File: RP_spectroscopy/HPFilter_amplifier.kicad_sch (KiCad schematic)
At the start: 0 parts

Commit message: Added components to the power supply branch. Implemented the Sallen-Key filter + amplification branch.
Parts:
- added C14, C15: 10n, symbol Device:C
- added R20, R21: 5K36, symbol Device:R
- added R22, R24: 1k, symbol Device:R
- added R23, R25: 7K32, symbol Device:R
- added R26: 49R9, symbol Device:R
- added U6: OPA1644, Package_SO:SOIC-14_3.9x8.7mm_P1.27mm, symbol Device:Opamp_Quad
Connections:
- new net: C14.2, C15.1, R20.1
- new net: C15.2, R21.1, U6.3 (+)
- new net: R22.1, R23.1, U6.6 (-)
- new net: R20.2, U6.1, U6.2 (-), U6.5 (+)
- new net: R23.2, U6.10 (+), U6.7
- new net: R25.2, R26.1, U6.8
- new net: R24.1, R25.1, U6.9 (-)
- new net +15V: U6.4 (V+)
- new net -15V: U6.11 (V-)
- new net GND: R21.2, R22.2, R24.2
- new net HPF + amplif: R26.2
- new net PD: C14.1
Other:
- note added: "Cascade amplification"
- note added: "Sallen-Key filter in HP configuration"

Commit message: Commit before deleting the VCO schematic from the main project. I have a separate project for that.
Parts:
- C14, C15: footprint (none) -> Capacitor_SMD:C_0805_2012Metric_Pad1.18x1.45mm_HandSolder
- R20, R21, R22, R23, R24, R25, R26: footprint (none) -> Resistor_SMD:R_0805_2012Metric_Pad1.20x1.40mm_HandSolder
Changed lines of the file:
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@@
 			)
 		)
-		(property "Footprint" ""
+		(property "Footprint" "Capacitor_SMD:C_0805_2012Metric_Pad1.18x1.45mm_HandSolder"
 			(at 101.6 79.0448 0)
 			(effects
@@
 			)
 		)
-		(property "Description" "Unpolarized capacitor"
+		(property "Description" "Unpolarized capacitor, 10n C0G 50V"
 			(at 97.79 80.01 0)
 			(effects
@@
 			)
 		)
-		(property "Footprint" ""
+		(property "Footprint" "Resistor_SMD:R_0805_2012Metric_Pad1.20x1.40mm_HandSolder"
 			(at 103.632 87.63 90)
 			(effects
@@
 			)
 		)
-		(property "Description" "Resistor"
+		(property "Description" "Resistor, 5k36 1%"
 			(at 105.41 87.63 0)
 			(effects
@@
 			)
 		)
-		(property "Footprint" ""
+		(property "Footprint" "Resistor_SMD:R_0805_2012Metric_Pad1.20x1.40mm_HandSolder"
 			(at 151.892 104.14 90)
 			(effects
@@
 			)
 		)
-		(property "Description" "Resistor"
+		(property "Description" "Resistor, 1k 1%"
 			(at 153.67 104.14 0)
 			(effects
@@
 			)
 		)
-		(property "Footprint" ""
+		(property "Footprint" "Resistor_SMD:R_0805_2012Metric_Pad1.20x1.40mm_HandSolder"
 			(at 217.17 89.408 90)
 			(effects
@@
 			)
 		)
-		(property "Description" "Resistor"
+		(property "Description" "Resistor, 49R9 1%"
 			(at 217.17 87.63 0)
 			(effects
@@
 			)
 		)
-		(property "Footprint" ""
+		(property "Footprint" "Resistor_SMD:R_0805_2012Metric_Pad1.20x1.40mm_HandSolder"
 			(at 200.66 100.838 90)
 			(effects
@@
 			)
 		)
-		(property "Description" "Resistor"
+		(property "Description" "Resistor, 7k32 1%"
 			(at 200.66 99.06 0)
 			(effects
@@
 			)
 		)
-		(property "Footprint" ""
+		(property "Footprint" "Resistor_SMD:R_0805_2012Metric_Pad1.20x1.40mm_HandSolder"
 			(at 113.03 71.628 90)
 			(effects
@@
 			)
 		)
-		(property "Description" "Resistor"
+		(property "Description" "Resistor, 5k36 1%"
 			(at 113.03 69.85 0)
 			(effects
@@
 			)
 		)
-		(property "Footprint" ""
+		(property "Footprint" "Capacitor_SMD:C_0805_2012Metric_Pad1.18x1.45mm_HandSolder"
 			(at 88.9 79.0448 0)
 			(effects
@@
 			)
 		)
-		(property "Description" "Unpolarized capacitor"
+		(property "Description" "Unpolarized capacitor, 10n C0G 50V"
 			(at 85.09 80.01 0)
 			(effects
@@
 			)
 		)
-		(property "Footprint" ""
+		(property "Footprint" "Resistor_SMD:R_0805_2012Metric_Pad1.20x1.40mm_HandSolder"
 			(at 181.102 106.68 90)
 			(effects
@@
 			)
 		)
-		(property "Description" "Resistor"
+		(property "Description" "Resistor, 1k 1%"
 			(at 182.88 106.68 0)
 			(effects
@@
 			)
 		)
-		(property "Footprint" ""
+		(property "Footprint" "Resistor_SMD:R_0805_2012Metric_Pad1.20x1.40mm_HandSolder"
 			(at 167.64 98.298 90)
 			(effects
@@
 			)
 		)
-		(property "Description" "Resistor"
+		(property "Description" "Resistor, 7k32 1%"
 			(at 167.64 96.52 0)
 			(effects

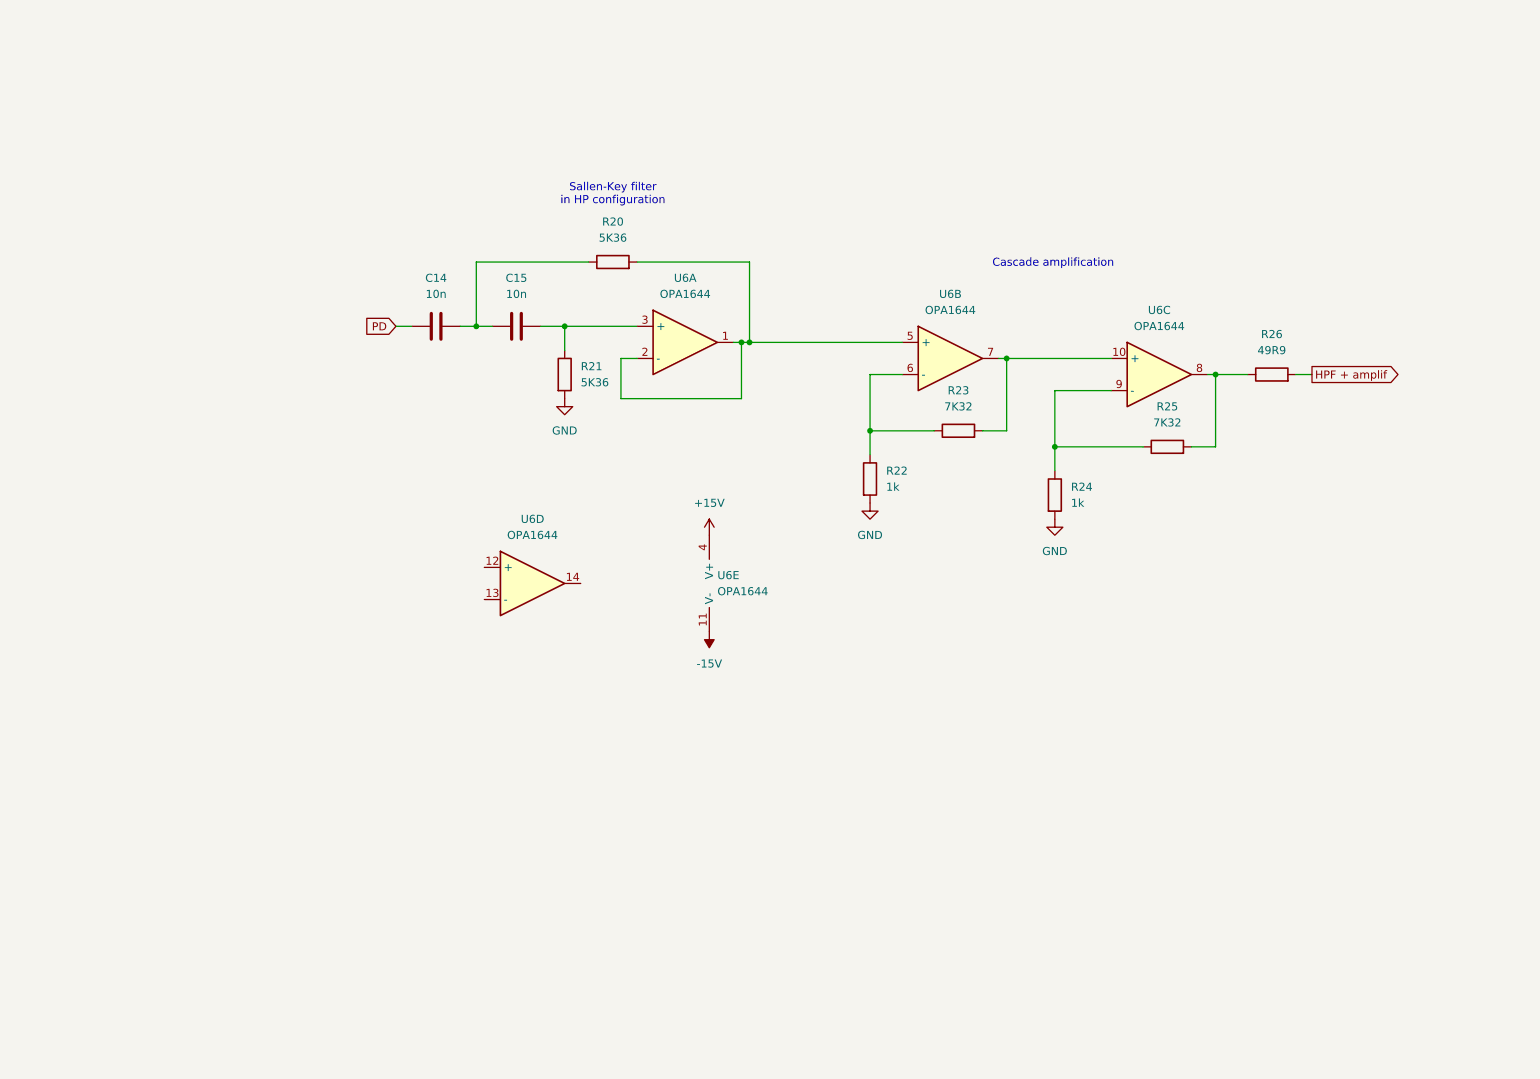
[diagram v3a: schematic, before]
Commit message: Changed the way of implementing the powerline capacitors in order to find them easily while creating the pcb. Started implementing the double Sallen-Key filter.
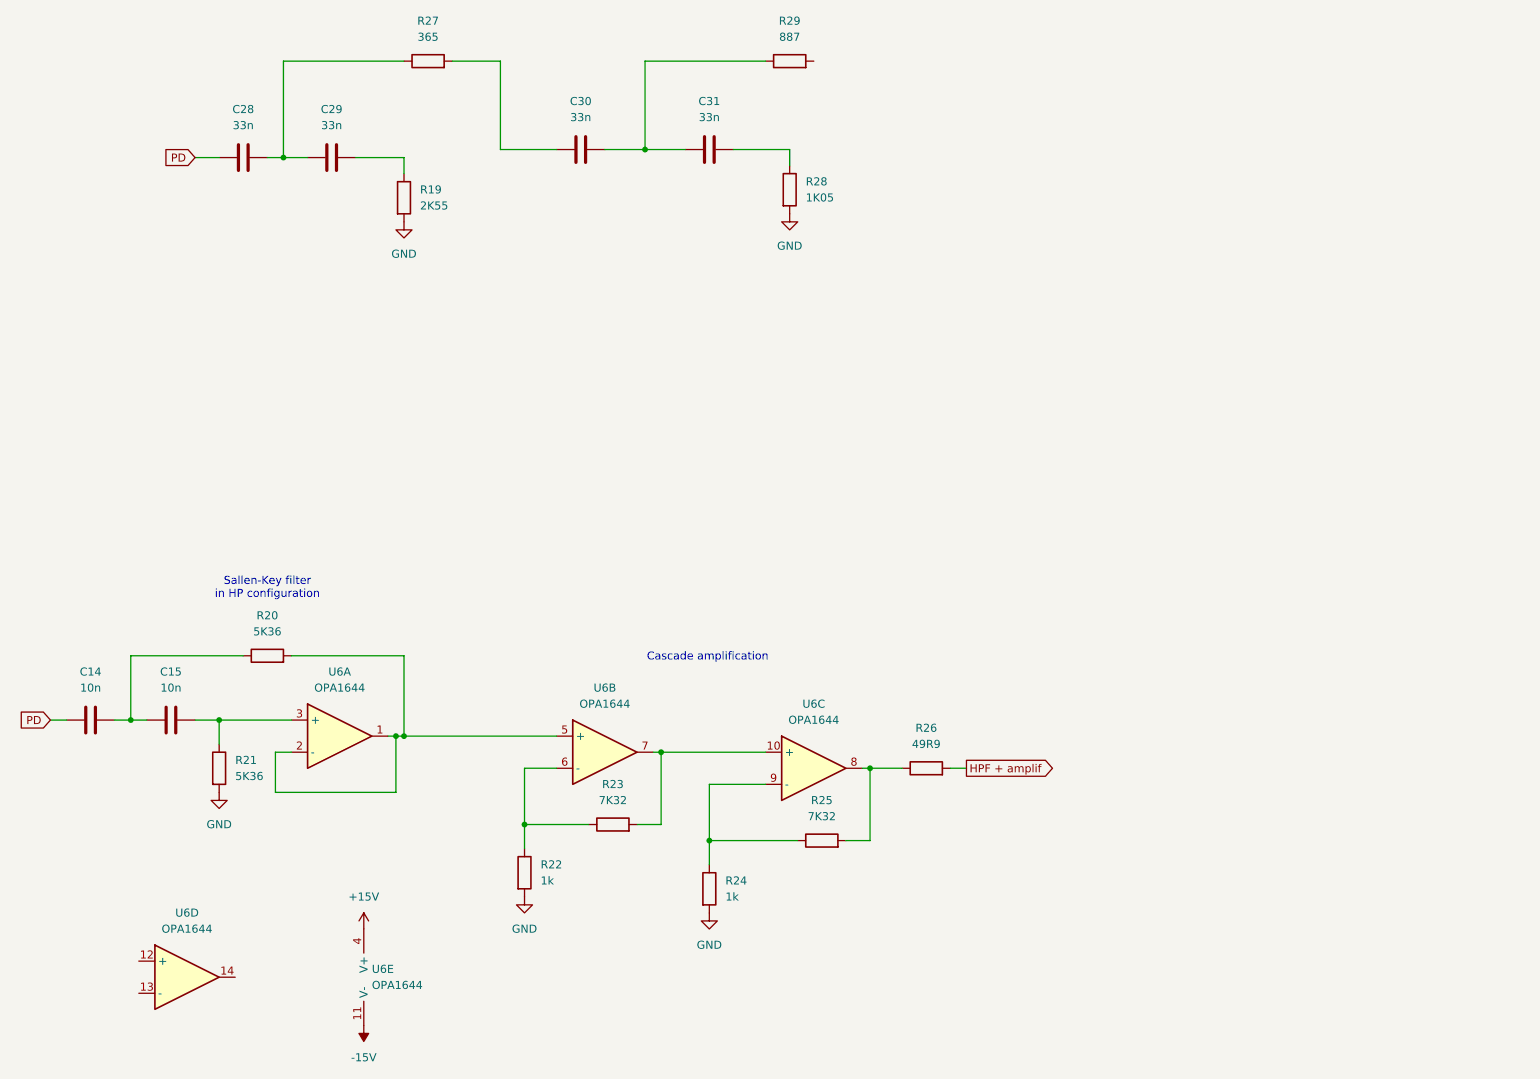
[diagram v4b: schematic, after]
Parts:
- added C28, C29, C30, C31: 33n, Capacitor_SMD:C_0805_2012Metric_Pad1.18x1.45mm_HandSolder, symbol Device:C
- added R19: 2K55, Resistor_SMD:R_0805_2012Metric_Pad1.20x1.40mm_HandSolder, symbol Device:R
- added R27: 365, Resistor_SMD:R_0805_2012Metric_Pad1.20x1.40mm_HandSolder, symbol Device:R
- added R28: 1K05, Resistor_SMD:R_0805_2012Metric_Pad1.20x1.40mm_HandSolder, symbol Device:R
- added R29: 887, Resistor_SMD:R_0805_2012Metric_Pad1.20x1.40mm_HandSolder, symbol Device:R
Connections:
- net GND: now also R19.2, R28.2
- net PD: now also C28.1
- new net: C29.2, R19.1
- new net: C31.2, R28.1
- new net: C28.2, C29.1, R27.1
- new net: C30.1, R27.2
- new net: C30.2, C31.1, R29.1
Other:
- moved on the sheet: C14, C15, R20, R21, R22, R23, R24, R25, R26, U6A, U6B, U6C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

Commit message: Added the summator parameters. Started to do the wireings
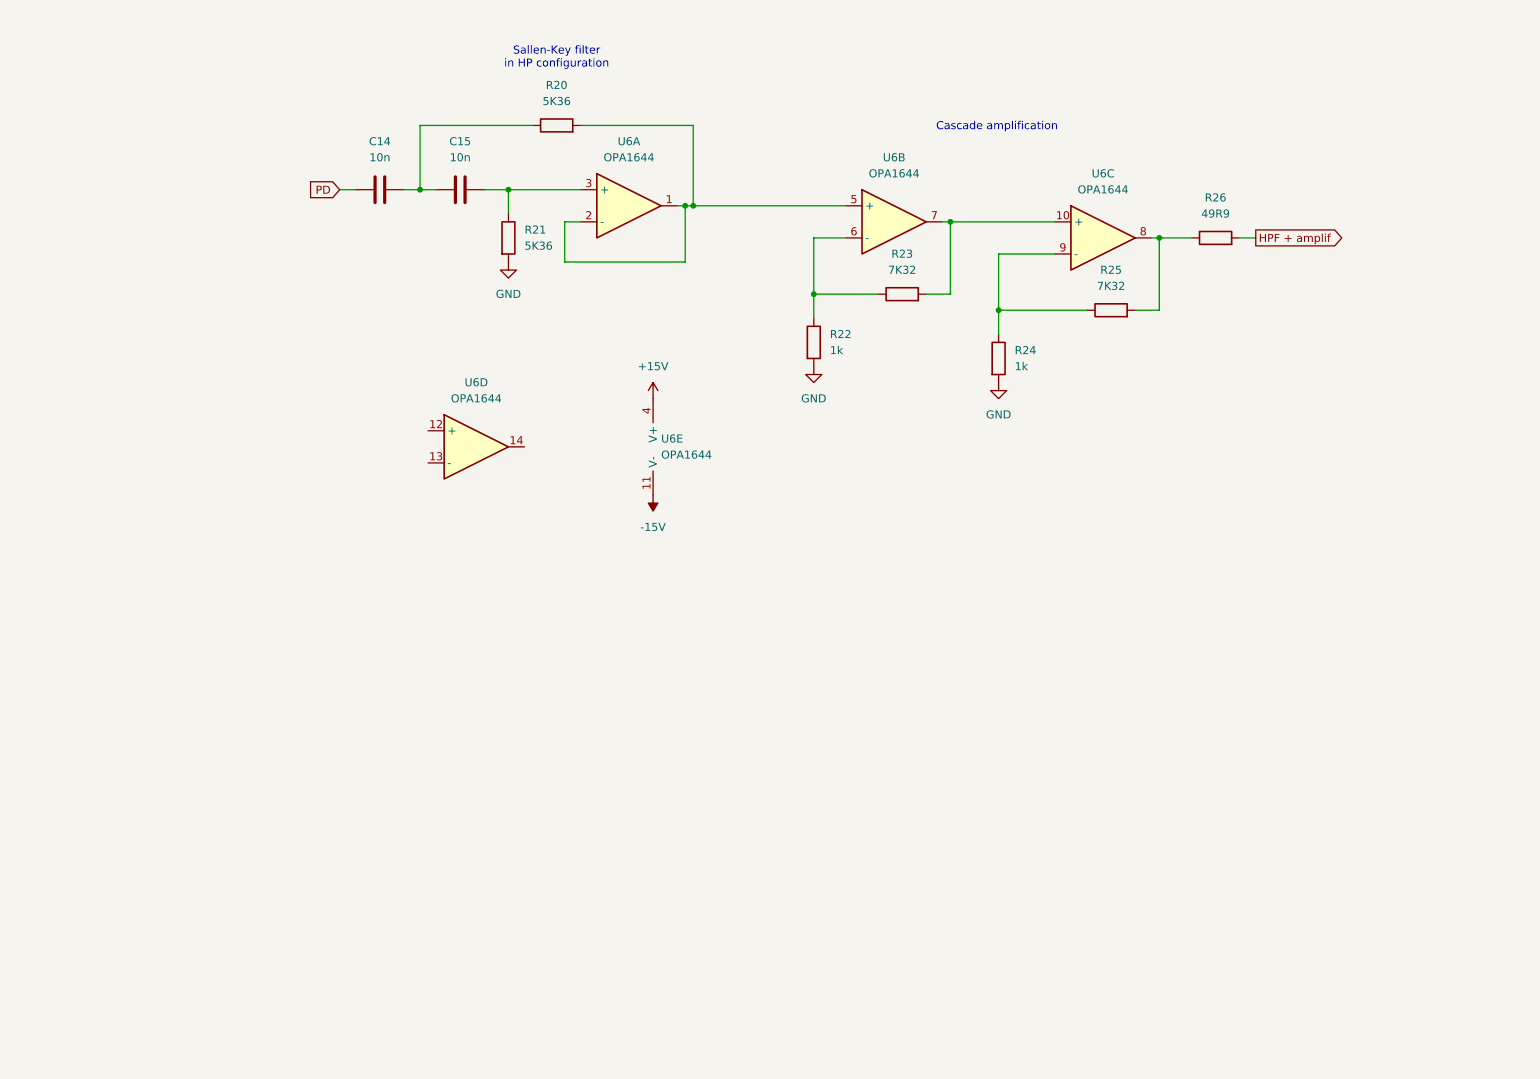
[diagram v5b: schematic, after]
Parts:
- removed C28, C29, C30, C31: 33n, Capacitor_SMD:C_0805_2012Metric_Pad1.18x1.45mm_HandSolder, symbol Device:C
- removed R19: 2K55, Resistor_SMD:R_0805_2012Metric_Pad1.20x1.40mm_HandSolder, symbol Device:R
- removed R27: 365, Resistor_SMD:R_0805_2012Metric_Pad1.20x1.40mm_HandSolder, symbol Device:R
- removed R28: 1K05, Resistor_SMD:R_0805_2012Metric_Pad1.20x1.40mm_HandSolder, symbol Device:R
- removed R29: 887, Resistor_SMD:R_0805_2012Metric_Pad1.20x1.40mm_HandSolder, symbol Device:R
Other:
- moved on the sheet: C14, C15, R20, R21, R22, R23, R24, R25, R26, U6A, U6B, U6C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

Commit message: Added the BP filter and the amplification stages. It should be done.
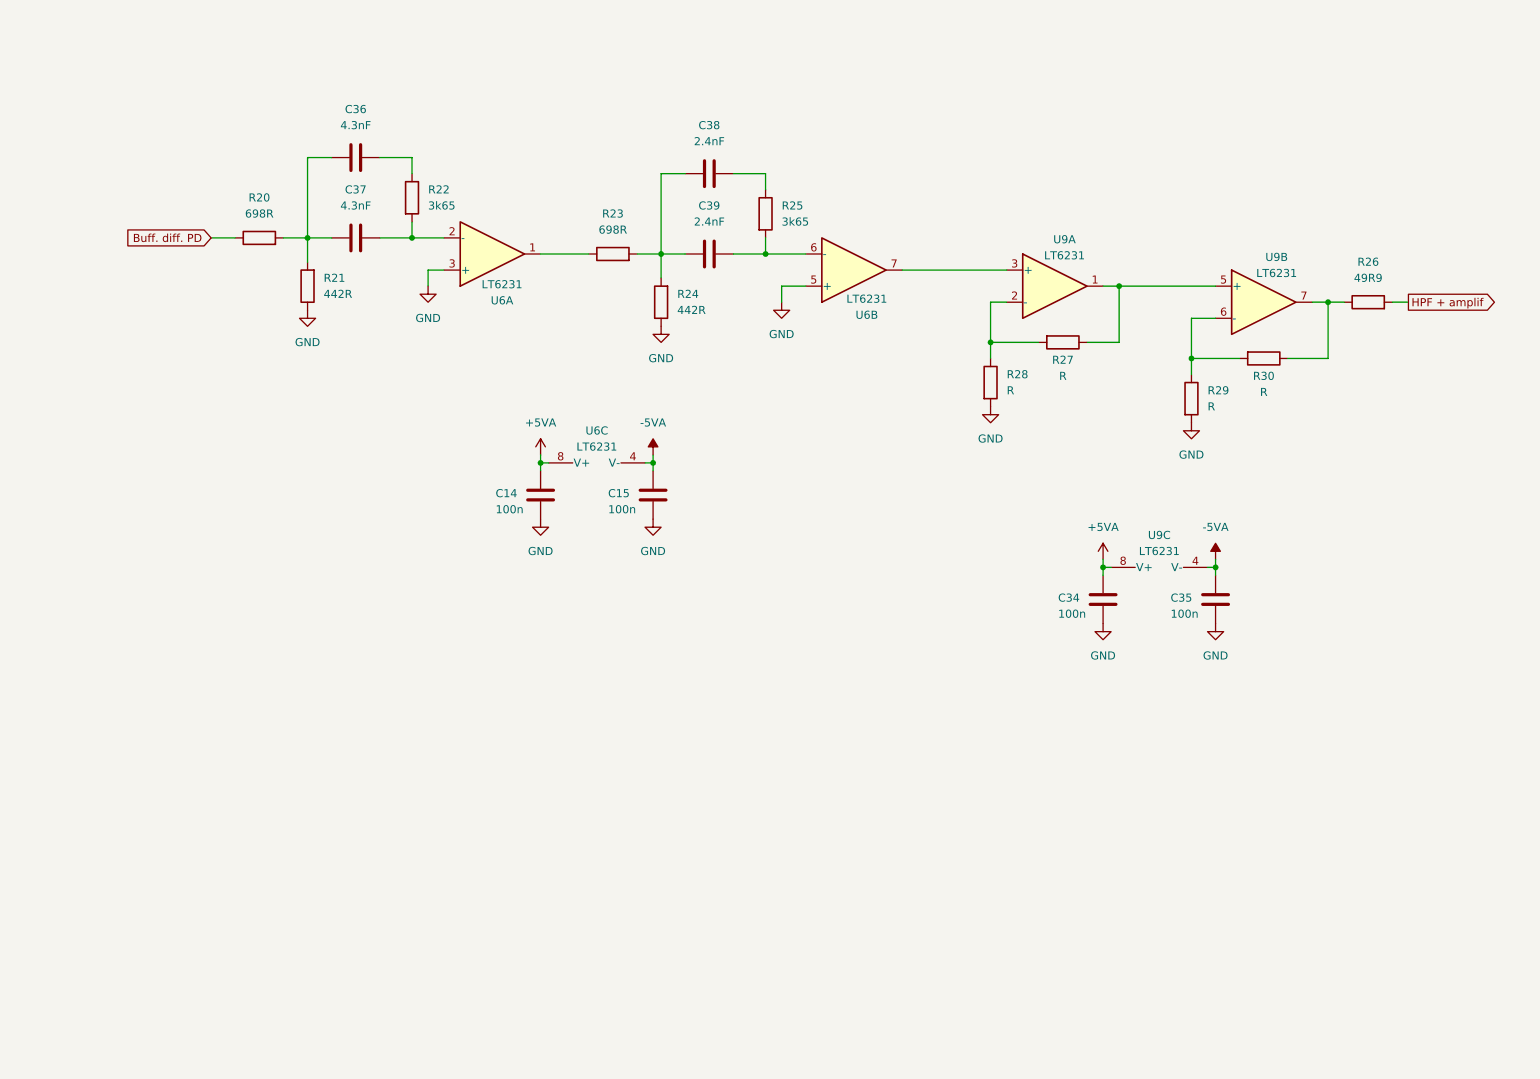
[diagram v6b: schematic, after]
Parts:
- removed U6: OPA1644, Package_SO:SOIC-14_3.9x8.7mm_P1.27mm, symbol Device:Opamp_Quad
- added C34, C35: 100n, Capacitor_SMD:C_0805_2012Metric_Pad1.18x1.45mm_HandSolder, symbol Device:C
- added C36, C37: 4.3nF, Capacitor_SMD:C_0805_2012Metric_Pad1.18x1.45mm_HandSolder, symbol Device:C
- added C38, C39: 2.4nF, Capacitor_SMD:C_0603_1608Metric_Pad1.08x0.95mm_HandSolder, symbol Device:C
- added R27, R28, R29, R30: R, Resistor_SMD:R_0805_2012Metric_Pad1.20x1.40mm_HandSolder, symbol Device:R
- added U6, U9: LT6231, Package_SO:SOIC-8_3.9x4.9mm_P1.27mm, symbol Amplifier_Operational:LT6234
- C14, C15: value 10n -> 100n
- R20: value 5K36 -> 698R
- R21: value 5K36 -> 442R
- R22: value 1k -> 3k65
- R23: value 7K32 -> 698R
- R24: value 1k -> 442R
- R25: value 7K32 -> 3k65
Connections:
- net GND: now also C14.2, C15.2, R21.1, R24.1, C34.2, C35.2, R28.2, R29.2, U6.3 (+), U6.5 (+); no longer R21.2, R22.2, R24.2
- net at R23.1: now also U6.1; no longer R22.1
- net at R20.2: now also R21.2, C36.1, C37.1
- net at R23.2: now also R24.2, C38.1, C39.1
- net at R25.2: now also C39.2, U6.6 (-); no longer R26.1
- net at R25.1: now also C38.2; no longer R24.1
- net PD renamed +5VA
- net +5VA: now also C34.1, U6.8 (V+), U9.8 (V+)
- new net: R26.1, R30.1, U9.7
- new net: R29.1, R30.2, U9.6 (-)
- new net: U6.7, U9.3 (+)
- new net: R27.2, R28.1, U9.2 (-)
- new net: R27.1, U9.1, U9.5 (+)
- new net: C36.2, R22.1
- new net: C37.2, R22.2, U6.2 (-)
- new net -5VA: C15.1, C35.1, U6.4 (V-), U9.4 (V-)
- new net Buff. diff. PD: R20.1
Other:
- note removed: "Cascade amplification"
- note removed: "Sallen-Key filter in HP configuration"
- moved on the sheet: R26
